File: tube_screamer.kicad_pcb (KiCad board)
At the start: 2 copper layers, 61 x 45 mm, 48 parts, among them Q1 MMBT5551, Q2 MMBT5551, Q3 MMBT5551, U1 NE5532

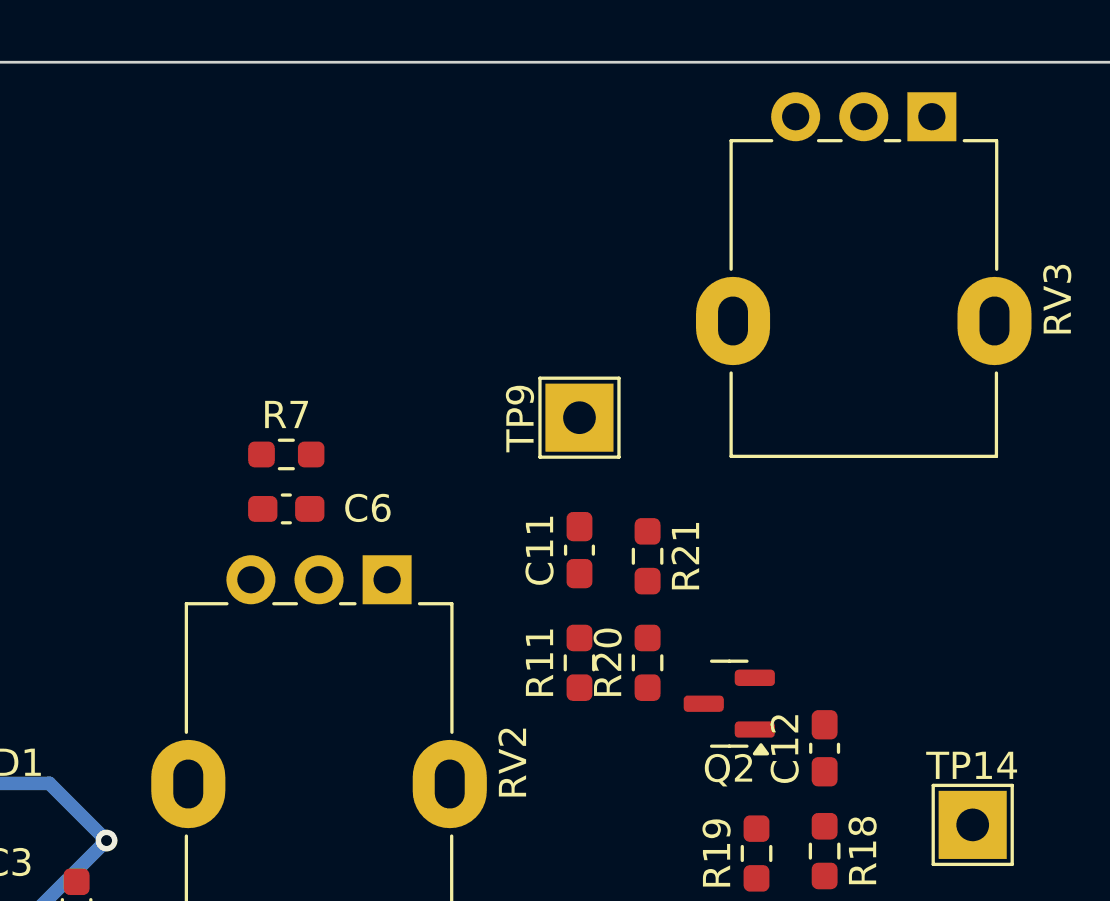
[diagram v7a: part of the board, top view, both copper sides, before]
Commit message: Updated switch, added diode.
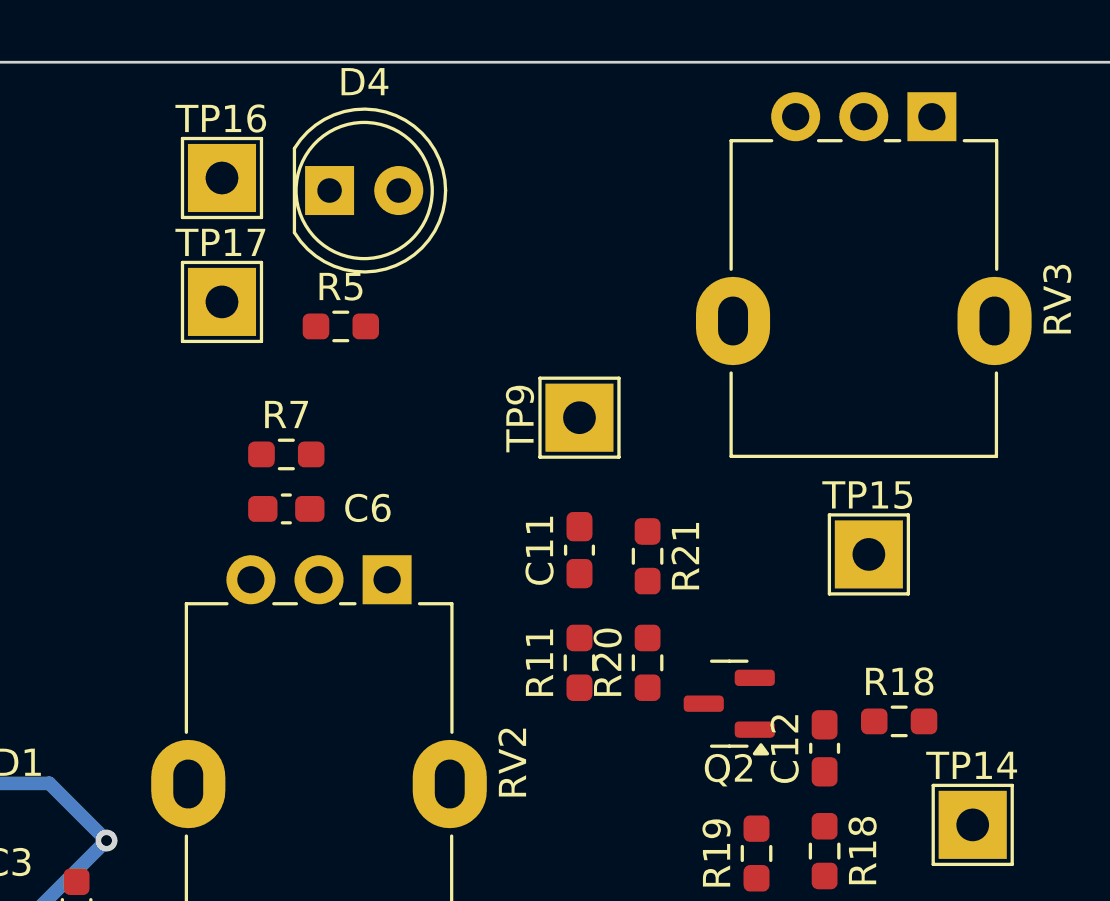
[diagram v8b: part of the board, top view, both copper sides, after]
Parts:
- added D4: LED, LED_THT:LED_D5.0mm, F.Cu at (130.4, 104.7)
- added R18: 0, Resistor_SMD:R_0603_1608Metric_Pad0.98x0.95mm_HandSolder, F.Cu at (151.3, 124.2)
- added R5: 1k, Resistor_SMD:R_0603_1608Metric_Pad0.98x0.95mm_HandSolder, F.Cu at (130.8, 109.7)
- added TP15: SW_ON, TestPoint:TestPoint_THTPad_2.5x2.5mm_Drill1.2mm, F.Cu at (150.2, 118.1)
- added TP16: DIODE_ON, TestPoint:TestPoint_THTPad_2.5x2.5mm_Drill1.2mm, F.Cu at (126.4, 104.2)
- added TP17: DIODE_SUPPLY, TestPoint:TestPoint_THTPad_2.5x2.5mm_Drill1.2mm, F.Cu at (126.4, 108.8)
- TP13: value bypass_in -> SW_OFF
- TP14: value bypass_out -> SW_MID
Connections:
- net Net-(Q1-E) renamed /SW_OFF
- C12 pad 1: Net-(C12-Pad1) -> /SW_MID
- RV3 pad 2: Net-(R18-Pad2) -> /SW_ON
- TP14 pad 1: Net-(C12-Pad1) -> /SW_MID
